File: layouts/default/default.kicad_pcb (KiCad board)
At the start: 2 copper layers, 31 parts

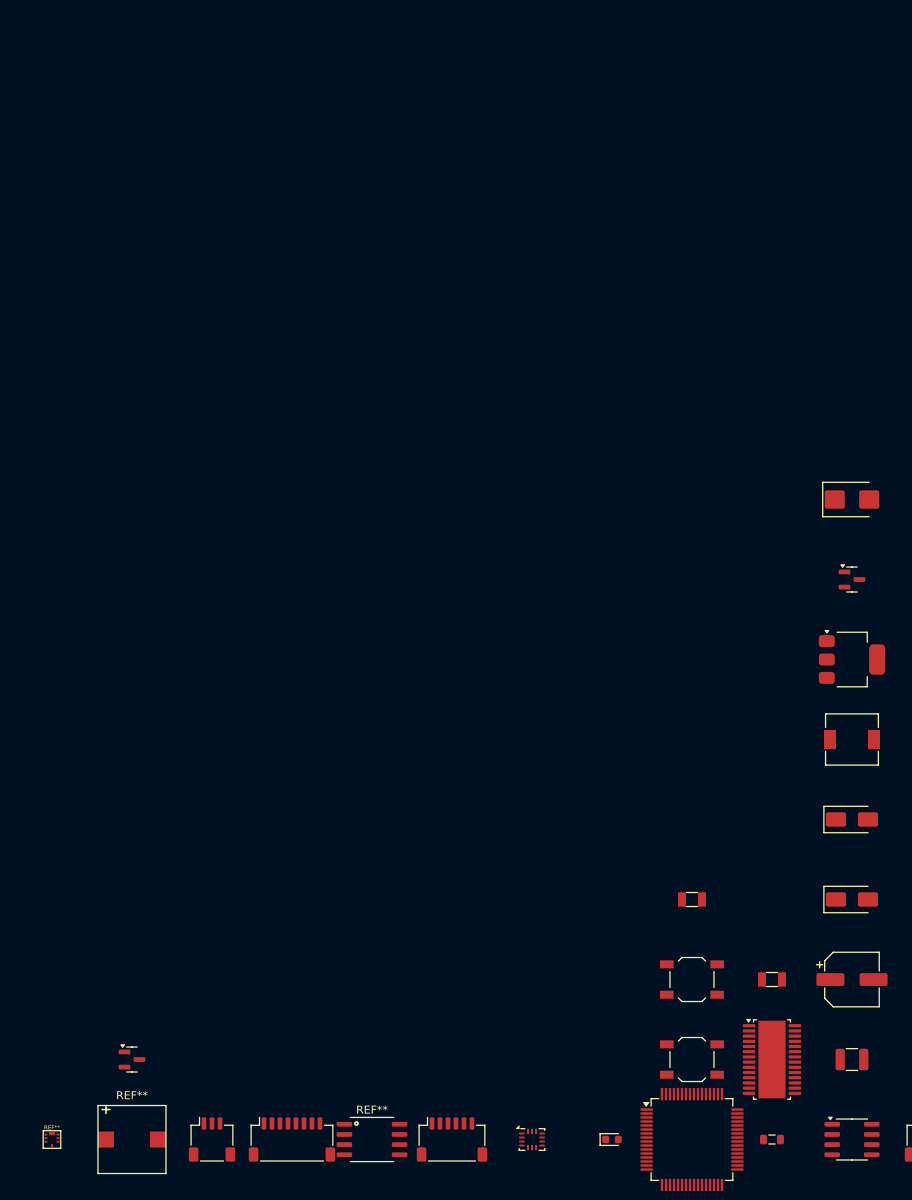
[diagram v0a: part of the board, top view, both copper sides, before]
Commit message: REV-005: Add footprints to all passive components — 91 parts now in KiCad PCB
Generic Resistor and Capacitor components had no footprint assignments,
causing 62 components to be excluded from the PCB netlist. Fixed by:

- Added default 0402 footprints to Resistor and Capacitor components
- Overrode to 0603 for VCAP 2.2uF caps, 0805 for 4.7-10uF, 1206 for 22uF
- Replaced generic ElectrolyticCap (no footprint) with pinned components:
  c_5v_bulk reuses Cap_100uF_35V, c_3v3_bulk/c_ldo_out use new
  Cap_22uF_10V_Tant (EIA-3528 Kemet-B tantalum for AMS1117 ESR stability)

Co-Authored-By: Claude Opus 4.6 <noreply@anthropic.com>
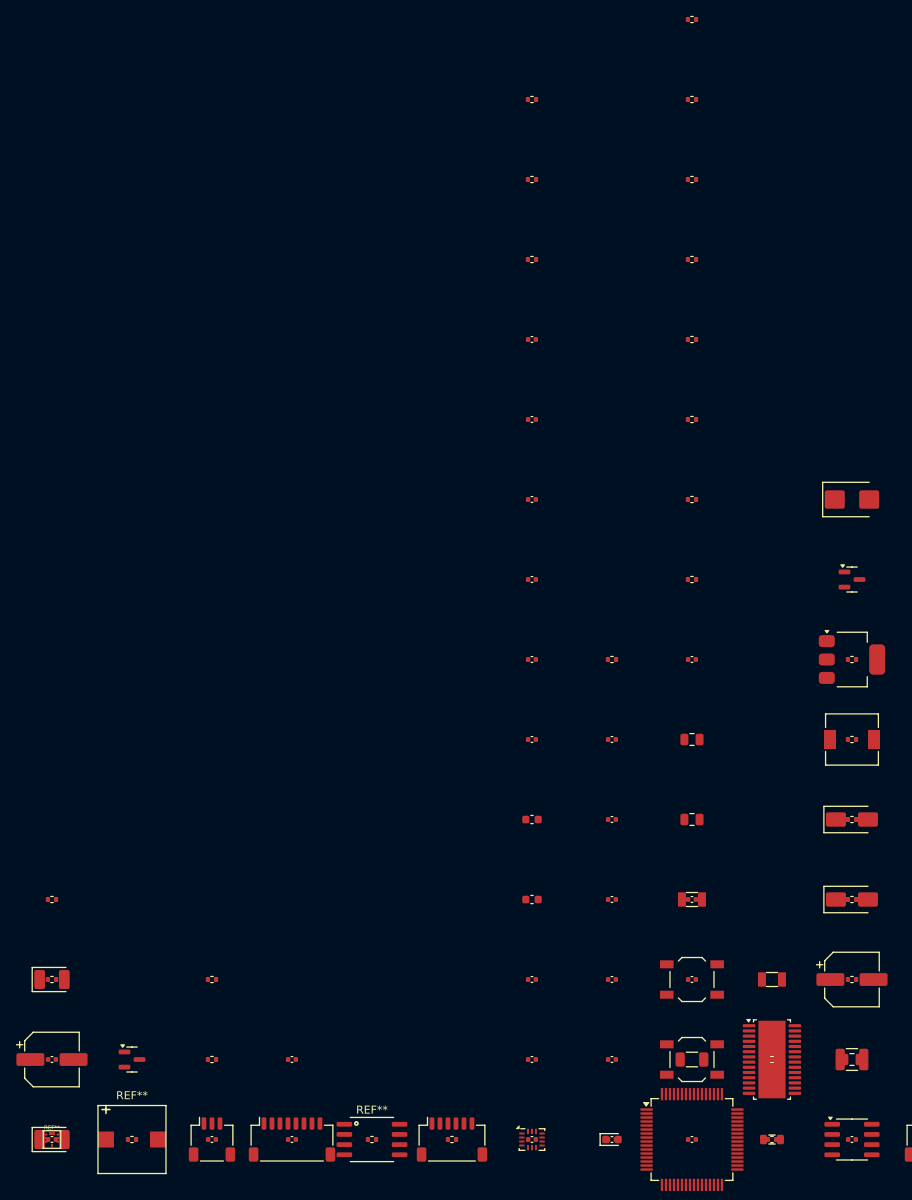
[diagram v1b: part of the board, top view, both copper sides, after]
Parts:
- added C10: , Capacitor_SMD:C_0402_1005Metric, F.Cu at (60.0, -20.0)
- added C11: , Capacitor_SMD:C_0603_1608Metric, F.Cu at (60.0, -30.0)
- added C12: , Capacitor_SMD:C_0603_1608Metric, F.Cu at (60.0, -40.0)
- added C13: , Capacitor_SMD:C_0402_1005Metric, F.Cu at (60.0, -50.0)
- added C14: , Capacitor_SMD:C_0402_1005Metric, F.Cu at (60.0, -60.0)
- added C15: , Capacitor_SMD:C_0402_1005Metric, F.Cu at (60.0, -70.0)
- added C16: , Capacitor_SMD:C_0402_1005Metric, F.Cu at (60.0, -80.0)
- added C17: , Capacitor_SMD:C_0402_1005Metric, F.Cu at (60.0, -90.0)
- added C18: , Capacitor_SMD:C_0402_1005Metric, F.Cu at (60.0, -100.0)
- added C19: , Capacitor_SMD:C_0402_1005Metric, F.Cu at (70.0, 0.00)
- added C20: , Capacitor_SMD:C_0402_1005Metric, F.Cu at (70.0, -10.0)
- added C21: , Capacitor_SMD:C_0402_1005Metric, F.Cu at (70.0, -20.0)
- added C22: , Capacitor_SMD:C_0402_1005Metric, F.Cu at (70.0, -30.0)
- added C23: , Capacitor_SMD:C_0402_1005Metric, F.Cu at (70.0, -40.0)
- added C24: , Capacitor_SMD:C_0402_1005Metric, F.Cu at (70.0, -50.0)
- added C25: , Capacitor_SMD:C_0402_1005Metric, F.Cu at (80.0, 0.00)
- added C26: , Capacitor_SMD:C_1206_3216Metric, F.Cu at (80.0, -10.0)
- added C27: , Capacitor_SMD:C_0402_1005Metric, F.Cu at (80.0, -20.0)
- added C28: , Capacitor_SMD:C_0402_1005Metric, F.Cu at (80.0, -30.0)
- added C29: , Capacitor_SMD:C_0805_2012Metric, F.Cu at (80.0, -40.0)
- added C3: , Capacitor_SMD:C_0402_1005Metric, F.Cu at (0.00, 0.00)
- added C30: , Capacitor_SMD:C_0805_2012Metric, F.Cu at (80.0, -50.0)
- added C31: , Capacitor_SMD:C_0402_1005Metric, F.Cu at (80.0, -60.0)
- added C32: , Capacitor_SMD:C_0402_1005Metric, F.Cu at (100.0, 0.00)
- added C33: , Capacitor_SMD:C_0805_2012Metric, F.Cu at (100.0, -10.0)
- added C34: , Capacitor_Tantalum_SMD:CP_EIA-3528-21_Kemet-B, F.Cu at (0.00, 0.00)
- added C35: , Capacitor_SMD:CP_Elec_6.3x7.7, F.Cu at (0.00, -10.0)
- added C36: , Capacitor_Tantalum_SMD:CP_EIA-3528-21_Kemet-B, F.Cu at (0.00, -20.0)
- added C4: , Capacitor_SMD:C_0402_1005Metric, F.Cu at (0.00, -10.0)
- added C5: , Capacitor_SMD:C_0402_1005Metric, F.Cu at (20.0, 0.00)
- added C6: , Capacitor_SMD:C_0402_1005Metric, F.Cu at (30.0, 0.00)
- added C7: , Capacitor_SMD:C_0402_1005Metric, F.Cu at (30.0, -10.0)
- added C8: , Capacitor_SMD:C_0402_1005Metric, F.Cu at (60.0, 0.00)
- added C9: , Capacitor_SMD:C_0402_1005Metric, F.Cu at (60.0, -10.0)
- added R1: , Resistor_SMD:R_0402_1005Metric, F.Cu at (0.00, -20.0)
- added R10: , Resistor_SMD:R_0402_1005Metric, F.Cu at (60.0, -130.0)
- added R11: , Resistor_SMD:R_0402_1005Metric, F.Cu at (70.0, -60.0)
- added R12: , Resistor_SMD:R_0402_1005Metric, F.Cu at (80.0, -70.0)
- added R13: , Resistor_SMD:R_0402_1005Metric, F.Cu at (80.0, -80.0)
- added R14: , Resistor_SMD:R_0402_1005Metric, F.Cu at (80.0, -90.0)
- added R15: , Resistor_SMD:R_0402_1005Metric, F.Cu at (80.0, -100.0)
- added R16: , Resistor_SMD:R_0402_1005Metric, F.Cu at (80.0, -110.0)
- added R17: , Resistor_SMD:R_0402_1005Metric, F.Cu at (80.0, -120.0)
- added R18: , Resistor_SMD:R_0402_1005Metric, F.Cu at (80.0, -130.0)
- added R19: , Resistor_SMD:R_0402_1005Metric, F.Cu at (80.0, -140.0)
- added R2: , Resistor_SMD:R_0402_1005Metric, F.Cu at (0.00, -30.0)
- added R20: , Resistor_SMD:R_0402_1005Metric, F.Cu at (90.0, 0.00)
- added R21: , Resistor_SMD:R_0402_1005Metric, F.Cu at (90.0, -10.0)
- added R22: , Resistor_SMD:R_0402_1005Metric, F.Cu at (100.0, -20.0)
- added R23: , Resistor_SMD:R_0402_1005Metric, F.Cu at (100.0, -30.0)
- added R24: , Resistor_SMD:R_0402_1005Metric, F.Cu at (100.0, -40.0)
- added R25: , Resistor_SMD:R_0402_1005Metric, F.Cu at (100.0, -50.0)
- added R26: , Resistor_SMD:R_0402_1005Metric, F.Cu at (100.0, -60.0)
- added R3: , Resistor_SMD:R_0402_1005Metric, F.Cu at (10.0, 0.00)
- added R4: , Resistor_SMD:R_0402_1005Metric, F.Cu at (20.0, -10.0)
- added R5: , Resistor_SMD:R_0402_1005Metric, F.Cu at (20.0, -20.0)
- added R6: , Resistor_SMD:R_0402_1005Metric, F.Cu at (40.0, 0.00)
- added R7: , Resistor_SMD:R_0402_1005Metric, F.Cu at (50.0, 0.00)
- added R8: , Resistor_SMD:R_0402_1005Metric, F.Cu at (60.0, -110.0)
- added R9: , Resistor_SMD:R_0402_1005Metric, F.Cu at (60.0, -120.0)
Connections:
- BZ1 pad 1: (no net) -> v5
- BZ1 pad 2: (no net) -> drain
- C1 pad 1: (no net) -> vbat
- C1 pad 2: (no net) -> baro-gnd
- C2 pad 1: (no net) -> vbat
- C2 pad 2: (no net) -> baro-gnd
- D1 pad 1: (no net) -> footprint-gpio-0
- D1 pad 2: (no net) -> anode
- D2 pad 1: (no net) -> baro-gnd
- D2 pad 2: (no net) -> cathode
- D3 pad 1: (no net) -> vbus
- D3 pad 2: (no net) -> v5
- D4 pad 1: (no net) -> baro-gnd
- D4 pad 2: (no net) -> vbat
- FB1 pad 1: (no net) -> vdd
- FB1 pad 2: (no net) -> avdd
- J1 pad 1: (no net) -> baro-gnd
- J1 pad 2: (no net) -> v5
- J1 pad 3: (no net) -> cam_conn-video_in
- J2 pad 1: (no net) -> baro-gnd
- J2 pad 2: (no net) -> vbat
- J2 pad 3: (no net) -> curr
- J2 pad 4: (no net) -> pc6
- J2 pad 5: (no net) -> pc7
- J2 pad 6: (no net) -> pc8
- J2 pad 7: (no net) -> pc9
- J2 pad 8: (no net) -> telem
- J3 pad 1: (no net) -> baro-gnd
- J3 pad 2: (no net) -> v5
- J3 pad 3: (no net) -> conn-tx-0
- J3 pad 4: (no net) -> conn-rx-0
- J3 pad 5: (no net) -> scl
- J3 pad 6: (no net) -> sda
- J4 pad 1: (no net) -> baro-gnd
- J4 pad 2: (no net) -> v5
- J4 pad 3: (no net) -> conn-rx-2
- J4 pad 4: (no net) -> conn-tx-2
- J5 pad 1: (no net) -> baro-gnd
- J5 pad 2: (no net) -> v5
- J5 pad 3: (no net) -> conn-tx-1
- J5 pad 4: (no net) -> conn-rx-1
- J5 pad 5: (no net) -> v5
- J5 pad 6: (no net) -> baro-gnd
- J6 pad A1: (no net) -> baro-gnd
- J6 pad A12: (no net) -> baro-gnd
- J6 pad A4: (no net) -> vbus
- J6 pad A5: (no net) -> A5
- J6 pad A6: (no net) -> conn_dp
- J6 pad A7: (no net) -> conn_dm
- J6 pad A8: (no net) -> A8
- J6 pad A9: (no net) -> vbus
- J6 pad B1: (no net) -> baro-gnd
- J6 pad B12: (no net) -> baro-gnd
- J6 pad B4: (no net) -> vbus
- J6 pad B5: (no net) -> B5
- J6 pad B6: (no net) -> conn_dp
- J6 pad B7: (no net) -> conn_dm
- J6 pad B8: (no net) -> B8
- J6 pad B9: (no net) -> vbus
- J6 pad S1: (no net) -> shield
- J7 pad 1: (no net) -> baro-gnd
- J7 pad 2: (no net) -> vbat_sw
- J7 pad 3: (no net) -> c_sag-video_in
- J7 pad 4: (no net) -> smart_audio
- L1 pad 1: (no net) -> cathode
- L1 pad 2: (no net) -> v5
- Q1 pad 1: (no net) -> beeper-gate
- Q1 pad 2: (no net) -> baro-gnd
- Q1 pad 3: (no net) -> drain
- Q2 pad 1: (no net) -> footprint-gate-0
- Q2 pad 2: (no net) -> vbat
- Q2 pad 3: (no net) -> vbat_sw
- Q3 pad 1: (no net) -> footprint-gate-1
- Q3 pad 2: (no net) -> baro-gnd
- Q3 pad 3: (no net) -> uart_rx
- SW1 pad 1: (no net) -> boot0
- SW1 pad 2: (no net) -> vdd
- SW2 pad 1: (no net) -> nrst
- SW2 pad 2: (no net) -> c_hse1-gnd
- U1 pad 1: (no net) -> vdd
- U1 pad 10: (no net) -> vdd
- U1 pad 2: (no net) -> scl
- U1 pad 3: (no net) -> baro-gnd
- U1 pad 4: (no net) -> sda
- U1 pad 5: (no net) -> vdd
- U1 pad 6: (no net) -> vdd
- U1 pad 7: (no net) -> int_out
- U1 pad 8: (no net) -> baro-gnd
- U1 pad 9: (no net) -> baro-gnd
- U2 pad 1: (no net) -> flash-cs
- U2 pad 2: (no net) -> flash-spi_miso
- U2 pad 3: (no net) -> wp
- U2 pad 4: (no net) -> baro-gnd
- U2 pad 5: (no net) -> flash-spi_mosi
- U2 pad 6: (no net) -> flash-spi_sck
- U2 pad 7: (no net) -> hold
- U2 pad 8: (no net) -> vdd
- U3 pad 1: (no net) -> footprint-spi_miso-0
- U3 pad 10: (no net) -> ocsb
- U3 pad 11: (no net) -> osdo
- U3 pad 12: (no net) -> footprint-cs-0
- U3 pad 13: (no net) -> footprint-spi_sck-0
- U3 pad 14: (no net) -> footprint-spi_mosi-0
- U3 pad 2: (no net) -> asdx
- U3 pad 3: (no net) -> ascx
- U3 pad 4: (no net) -> exti
- U3 pad 5: (no net) -> vdd
- U3 pad 6: (no net) -> baro-gnd
- U3 pad 7: (no net) -> baro-gnd
- U3 pad 8: (no net) -> vdd
- U3 pad 9: (no net) -> int2
- U4 pad 1: (no net) -> vdd
- U4 pad 10: (no net) -> adc_vbat
- U4 pad 12: (no net) -> c_hse1-gnd
- U4 pad 13: (no net) -> vdd
- U4 pad 14: (no net) -> pa0
- U4 pad 15: (no net) -> telem
- U4 pad 16: (no net) -> conn-tx-0
- U4 pad 17: (no net) -> conn-rx-0
- U4 pad 18: (no net) -> c_hse1-gnd
- U4 pad 19: (no net) -> vdd
- U4 pad 20: (no net) -> footprint-gpio-1
- U4 pad 21: (no net) -> footprint-spi_sck-0
- U4 pad 22: (no net) -> footprint-spi_miso-0
- U4 pad 23: (no net) -> footprint-spi_mosi-0
- U4 pad 24: (no net) -> footprint-cs-0
- U4 pad 25: (no net) -> exti
- U4 pad 26: (no net) -> footprint-gpio-0
- U4 pad 27: (no net) -> beeper-gpio
- U4 pad 28: (no net) -> pb2
- U4 pad 29: (no net) -> conn-tx-1
- U4 pad 30: (no net) -> conn-rx-1
- U4 pad 31: (no net) -> vcap1
- U4 pad 32: (no net) -> vdd
- U4 pad 33: (no net) -> footprint-cs-1
- U4 pad 34: (no net) -> footprint-spi_sck-1
- U4 pad 35: (no net) -> footprint-spi_miso-1
- U4 pad 36: (no net) -> footprint-spi_mosi-1
- U4 pad 37: (no net) -> pc6
- U4 pad 38: (no net) -> pc7
- U4 pad 39: (no net) -> pc8
- U4 pad 40: (no net) -> pc9
- U4 pad 41: (no net) -> pa8
- U4 pad 42: (no net) -> conn-tx-2
- U4 pad 43: (no net) -> uart_rx
- U4 pad 44: (no net) -> dm
- U4 pad 45: (no net) -> dp
- U4 pad 46: (no net) -> pa13
- U4 pad 47: (no net) -> vcap2
- U4 pad 48: (no net) -> vdd
- U4 pad 49: (no net) -> pa14
- U4 pad 5: (no net) -> xin
- U4 pad 50: (no net) -> pa15
- U4 pad 51: (no net) -> flash-spi_sck
- U4 pad 52: (no net) -> flash-spi_miso
- U4 pad 53: (no net) -> smart_audio
- U4 pad 54: (no net) -> pd2
- U4 pad 55: (no net) -> cam_ctrl-gpio
- U4 pad 57: (no net) -> flash-spi_mosi
- U4 pad 58: (no net) -> data
- U4 pad 59: (no net) -> flash-cs
- U4 pad 6: (no net) -> xout
- U4 pad 60: (no net) -> boot0
- U4 pad 61: (no net) -> scl
- U4 pad 62: (no net) -> sda
- U4 pad 63: (no net) -> c_hse1-gnd
- U4 pad 64: (no net) -> vdd
- U4 pad 7: (no net) -> nrst
- U4 pad 8: (no net) -> pc0
- U4 pad 9: (no net) -> adc_curr
- U5 pad 10: (no net) -> baro-gnd
- U5 pad 11: (no net) -> reset
- U5 pad 12: (no net) -> hsync
- U5 pad 13: (no net) -> vsync
- U5 pad 16: (no net) -> los
- U5 pad 17: (no net) -> footprint-spi_miso-1
- U5 pad 18: (no net) -> footprint-spi_sck-1
- U5 pad 19: (no net) -> footprint-spi_mosi-1
- U5 pad 20: (no net) -> footprint-cs-1
- U5 pad 21: (no net) -> clkout
- U5 pad 22: (no net) -> xfb
- U5 pad 23: (no net) -> clkin
- U5 pad 24: (no net) -> baro-gnd
- U5 pad 25: (no net) -> vdd
- U5 pad 29: (no net) -> baro-gnd
- U5 pad 3: (no net) -> c_sag-video_in
- U5 pad 4: (no net) -> sag
- U5 pad 5: (no net) -> vdd
- U5 pad 6: (no net) -> baro-gnd
- U5 pad 8: (no net) -> cam_conn-video_in
- U5 pad 9: (no net) -> avdd
- U6 pad 1: (no net) -> cathode
- U6 pad 2: (no net) -> vbat
- U6 pad 3: (no net) -> comp
- U6 pad 4: (no net) -> fb
- U6 pad 5: (no net) -> baro-gnd
- U6 pad 6: (no net) -> freq
- U6 pad 7: (no net) -> vbat
- U6 pad 8: (no net) -> bst
- U7 pad 1: (no net) -> baro-gnd
- U7 pad 2: (no net) -> vdd
- U7 pad 3: (no net) -> v5
- U8 pad 1: (no net) -> conn_dm
- U8 pad 2: (no net) -> conn_dm
- U8 pad 3: (no net) -> baro-gnd
- U8 pad 4: (no net) -> vbus
- U8 pad 5: (no net) -> conn_dp
- U8 pad 6: (no net) -> conn_dp
- Y1 pad 1: (no net) -> xin
- Y1 pad 2: (no net) -> xout
- Y2 pad 1: (no net) -> clkin
- Y2 pad 2: (no net) -> xfb

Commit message: REV-007: Add 10V VTX BEC and upgrade VTX connector to 5-pin
Add dedicated 10V/2A MP1584EN buck converter for VTX power, matching the
Brave F7 reference design. Upgrade VTX connector from 4-pin to 5-pin JST-SH
with full UART5 (TX+RX) for bidirectional VTX control (IRC Tramp, SmartAudio
v2.1). Redesign PINIO1 with 2N7002 N-FET level shifter for proper P-FET gate
drive at 10V source. Fix pre-existing duplicate REF** designators in PCB.

Co-Authored-By: Claude Opus 4.6 <noreply@anthropic.com>
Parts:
- removed U2: , lib:SOIC-8_5.23x5.23mm_P1.27mm
- added C37: , Capacitor_SMD:C_0402_1005Metric, F.Cu at (0.00, -10.0)
- added C38: , Capacitor_SMD:C_1210_3225Metric, F.Cu at (0.00, -20.0)
- added C39: , Capacitor_SMD:C_1206_3216Metric, F.Cu at (0.00, -30.0)
- added C40: , Capacitor_SMD:C_0402_1005Metric, F.Cu at (0.00, -40.0)
- added D5: , Diode_SMD:D_SMA, F.Cu at (0.00, -50.0)
- added L2: , Inductor_SMD:L_6.3x6.3_H3, F.Cu at (0.00, -60.0)
- added Q4: , Package_TO_SOT_SMD:SOT-23, F.Cu at (0.00, -70.0)
- added R27: , Resistor_SMD:R_0402_1005Metric, F.Cu at (0.00, -80.0)
- added R28: , Resistor_SMD:R_0402_1005Metric, F.Cu at (0.00, -90.0)
- added R29: , Resistor_SMD:R_0402_1005Metric, F.Cu at (0.00, -100.0)
- added R30: , Resistor_SMD:R_0402_1005Metric, F.Cu at (0.00, -110.0)
- added R31: , Resistor_SMD:R_0402_1005Metric, F.Cu at (0.00, -120.0)
- added U10: , lib:SOIC-8_5.23x5.23mm_P1.27mm, F.Cu at (112.5, 53.9)
- added U9: , lib:Bosch_LGA-10_2x2mm_P0.275x0.250mm, F.Cu at (100.3, 84.3)
- C1: footprint Capacitor_SMD:C_1210_3225Metric -> Capacitor_SMD:C_0402_1005Metric
- C10, C9: footprint Capacitor_SMD:C_0402_1005Metric -> Capacitor_SMD:C_0603_1608Metric
- C11, C12: footprint Capacitor_SMD:C_0603_1608Metric -> Capacitor_SMD:C_0402_1005Metric
- C2, C35: footprint Capacitor_SMD:CP_Elec_6.3x7.7 -> Capacitor_SMD:C_0402_1005Metric
- C23, C31: footprint Capacitor_SMD:C_0402_1005Metric -> Capacitor_Tantalum_SMD:CP_EIA-3528-21_Kemet-B
- C24: footprint Capacitor_SMD:C_0402_1005Metric -> Capacitor_SMD:CP_Elec_6.3x7.7
- C26: footprint Capacitor_SMD:C_1206_3216Metric -> Capacitor_SMD:C_1210_3225Metric
- C27: footprint Capacitor_SMD:C_0402_1005Metric -> Capacitor_SMD:C_1206_3216Metric
- C29: footprint Capacitor_SMD:C_0805_2012Metric -> Capacitor_SMD:C_0402_1005Metric
- C32: footprint Capacitor_SMD:C_0402_1005Metric -> Capacitor_SMD:C_0805_2012Metric
- C33: footprint Capacitor_SMD:C_0805_2012Metric -> Capacitor_SMD:CP_Elec_6.3x7.7
- C34: footprint Capacitor_Tantalum_SMD:CP_EIA-3528-21_Kemet-B -> Capacitor_SMD:C_0402_1005Metric
- C36: footprint Capacitor_Tantalum_SMD:CP_EIA-3528-21_Kemet-B -> Capacitor_SMD:C_0805_2012Metric
- J1: footprint Connector_JST:JST_SH_SM03B-SRSS-TB_1x03-1MP_P1.00mm_Horizontal -> Connector_JST:JST_SH_SM05B-SRSS-TB_1x05-1MP_P1.00mm_Horizontal
- J7: footprint Connector_JST:JST_SH_SM04B-SRSS-TB_1x04-1MP_P1.00mm_Horizontal -> Connector_JST:JST_SH_SM05B-SRSS-TB_1x05-1MP_P1.00mm_Horizontal
- U1: footprint lib:Bosch_LGA-10_2x2mm_P0.275x0.250mm -> Package_SO:SOIC-8_3.9x4.9mm_P1.27mm
- moved R19 210.4 mm to (121.6, 66.3)
- moved R10 201.1 mm to (118.7, 62.3)
- moved R18 198.7 mm to (121.6, 64.3)
- moved R9 189.6 mm to (118.7, 60.3)
- moved R17 187.0 mm to (121.6, 62.3)
- moved R8 178.3 mm to (118.7, 58.3)
- moved C18 176.2 mm to (133.1, 60.3)
- moved R16 175.3 mm to (121.6, 60.3)
- moved C16 165.8 mm to (130.3, 70.1)
- moved C17 165.4 mm to (133.1, 58.3)
- moved R14 164.9 mm to (118.7, 70.3)
- moved R15 163.7 mm to (121.6, 58.3)
- moved BZ1 155.2 mm to (138.0, 87.8)
- moved C15 155.0 mm to (130.3, 68.2)
- moved C35 154.9 mm to (136.0, 64.2)
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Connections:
- net drain renamed beeper-drain
- net uart_rx renamed footprint-uart_rx
- C1 pad 1: vbat -> vdd
- C10 pad 1: nrst -> vcap2
- C11 pad 1: vcap1 -> vdd
- C12 pad 1: vcap2 -> vdd
- C17 pad 1: vdd -> avdd
- C17 pad 2: c_hse1-gnd -> baro-gnd
- C18 pad 2: c_hse1-gnd -> baro-gnd
- C19 pad 1: avdd -> vdd
- C2 pad 1: vbat -> vdd
- C20 pad 1: vdd -> sag
- C20 pad 2: baro-gnd -> c_sag-video_in
- C21 pad 1: vdd -> clkin
- C22 pad 1: sag -> xfb
- C22 pad 2: c_sag-video_in -> baro-gnd
- C23 pad 1: clkin -> vdd
- C24 pad 1: xfb -> v5
- C26 pad 1: v5 -> vbat
- C27 pad 1: _1 -> v5
- C28 pad 1: adc_curr -> _1
- C29 pad 1: v5 -> adc_curr
- C31 pad 1: adc_vbat -> vdd
- C32 pad 1: shield -> v5
- C33 pad 1: vbus -> vbat
- C34 pad 1: vdd -> adc_vbat
- C35 pad 1: v5 -> shield
- C36 pad 1: vdd -> vbus
- C6 pad 1: vdd -> xin
- C6 pad 2: baro-gnd -> c_hse1-gnd
- C7 pad 1: vdd -> xout
- C7 pad 2: baro-gnd -> c_hse1-gnd
- C8 pad 1: xin -> nrst
- C9 pad 1: xout -> vcap1
- J7 pad 1: baro-gnd -> vtx_10v
- J7 pad 2: vbat_sw -> baro-gnd
- J7 pad 4: smart_audio -> conn-uart_rx
- Q2 pad 1: footprint-gate-0 -> footprint-drain
- Q2 pad 2: vbat -> rail_10v
- Q2 pad 3: vbat_sw -> vtx_10v
- U1 pad 1: vdd -> (no net)
- U1 pad 2: scl -> vbat
- U1 pad 3: baro-gnd -> (no net)
- U1 pad 4: sda -> (no net)
- U1 pad 5: vdd -> baro-gnd
- U1 pad 6: vdd -> (no net)
- U1 pad 7: int_out -> vbat
- U1 pad 8: baro-gnd -> (no net)
- U4 pad 53: smart_audio -> uart_tx
- U4 pad 54: pd2 -> conn-uart_rx
- U4 pad 55: cam_ctrl-gpio -> cam_ctrl
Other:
- board outline added: 36 x 36 mm

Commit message: REV-008: Replace cylindrical electrolytics with flat MLCCs
Remove all tall cylindrical aluminum electrolytic capacitors to match Brave F7
flat profile. VBAT bulk: 1x 100uF/35V electrolytic → 2x 22uF/35V MLCC (1210).
5V bulk: 1x 100uF/35V electrolytic → 2x 22uF/16V MLCC (1206). Removed unused
Cap_100uF_35V component definition.

Co-Authored-By: Claude Opus 4.6 <noreply@anthropic.com>
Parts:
- added C41: , Capacitor_SMD:C_1210_3225Metric, F.Cu at (0.00, -20.0)
- added C42: , Capacitor_SMD:C_1210_3225Metric, F.Cu at (0.00, -30.0)
- C24, C33: footprint Capacitor_SMD:CP_Elec_6.3x7.7 -> Capacitor_SMD:C_1206_3216Metric
- moved C37 161.4 mm to (62.5, 138.8)
- moved C38 161.4 mm to (62.5, 128.8)
- moved C39 161.4 mm to (62.5, 118.8)
- moved C40 161.4 mm to (62.5, 108.8)
- moved D5 161.4 mm to (62.5, 98.8)
- moved L2 161.4 mm to (62.5, 88.8)
- moved Q4 161.4 mm to (62.5, 78.8)
- moved R27 161.4 mm to (62.5, 68.8)
- moved R28 161.4 mm to (62.5, 58.8)
- moved R29 161.4 mm to (62.5, 48.8)
- moved R30 161.4 mm to (62.5, 38.8)
- moved R31 161.4 mm to (62.5, 28.8)
- moved U1 161.4 mm to (62.5, 148.8)
- moved C33 126.4 mm to (0.00, -10.0)
- moved C24 115.9 mm to (0.00, 0.00)
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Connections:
- net _1 renamed c_comp-_1
- net bst renamed buck-bst
- net cathode renamed buck-cathode
- net comp renamed buck-comp
- net fb renamed buck-fb
- net freq renamed buck-freq
- C33 pad 1: vbat -> v5
- C37 pad 1: (no net) -> buck_10v-bst
- C37 pad 2: (no net) -> buck_10v-cathode
- C40 pad 1: (no net) -> c_comp_10v-_1
- D5 pad 2: (no net) -> buck_10v-cathode
- L2 pad 1: (no net) -> buck_10v-cathode
- R27 pad 1: (no net) -> buck_10v-comp
- R27 pad 2: (no net) -> c_comp_10v-_1
- R28 pad 1: (no net) -> buck_10v-fb
- R29 pad 2: (no net) -> buck_10v-fb
- R30 pad 1: (no net) -> buck_10v-freq
- U1 pad 1: (no net) -> buck_10v-cathode
- U1 pad 3: (no net) -> buck_10v-comp
- U1 pad 4: (no net) -> buck_10v-fb
- U1 pad 6: (no net) -> buck_10v-freq
- U1 pad 8: (no net) -> buck_10v-bst

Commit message: REV-008: Single smaller boot button — Omron B3U-1000P replaces dual TL3342
Remove dedicated NRST button, replace BOOT0 button with compact Omron B3U-1000P
(3.0x2.5mm) to match Brave F7 reference. NRST pullup and debounce cap retained.
Saves ~0.21g, frees board space.

Co-Authored-By: Claude Opus 4.6 <noreply@anthropic.com>
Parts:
- removed SW2: , Button_Switch_SMD:SW_SPST_TL3342
- SW1: footprint Button_Switch_SMD:SW_SPST_TL3342 -> Button_Switch_SMD:SW_SPST_B3U-1000P

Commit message: Add persistent M3 mounting holes to ato source
Define MountingHole_M3 component (NPTH, no pad, no electrical connection)
matching Brave F7 reference. Four instances (H1-H4) in tf405.ato survive
ato build instead of being stripped from the PCB.

Co-Authored-By: Claude Opus 4.6 <noreply@anthropic.com>
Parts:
- added H1: , MountingHole:MountingHole_3.2mm_M3, F.Cu at (0.00, 0.00)
- added H2: , MountingHole:MountingHole_3.2mm_M3, F.Cu at (0.00, -10.0)
- added H3: , MountingHole:MountingHole_3.2mm_M3, F.Cu at (0.00, -20.0)
- added H4: , MountingHole:MountingHole_3.2mm_M3, F.Cu at (0.00, -30.0)
- moved SW1 54.6 mm to (97.0, 119.8)
